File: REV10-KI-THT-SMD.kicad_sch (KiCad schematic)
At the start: 40 parts, among them J1 EJ508A (PWR), J2 54-00298, P1 SPADE, P2 SPADE, Q1 2N3904, U1 NJM78M05FA, U2 LMC555CN, U3 STQ1HNK60R-AP, U4 STQ1HNK60R-AP, U5 TL5001AIP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

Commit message: first dual
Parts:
- C8: footprint THT-SMD:C_THT_SMD -> THT-SMD:CHV
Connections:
- net FINAL_SIGNAL: now also U6.P$6; no longer U6.P$17
- net GND: now also U6.P$26; no longer U6.P$10, U6.P$16
- no-connect marks 26 -> 27
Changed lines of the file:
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@@
 	)
 	(no_connect
-		(at 229.87 78.74)
+		(at 229.87 88.9)
 	)
 	(no_connect
-		(at 257.81 91.44)
+		(at 257.81 66.04)
 	)
 	(no_connect
@@
 		(at 229.87 91.44)
 	)
+	(no_connect
+		(at 257.81 68.58)
+	)
 	(wire
 		(pts
@@
 	(wire
 		(pts
-			(xy 257.81 66.04) (xy 260.35 66.04)
-		)
-		(stroke
-			(width 0)
-			(type default)
-		)
-	)
-	(wire
-		(pts
 			(xy 87.63 88.9) (xy 87.63 97.79)
 		)
@@
 	(wire
 		(pts
-			(xy 257.81 68.58) (xy 261.62 68.58)
-		)
-		(stroke
-			(width 0)
-			(type default)
-		)
-	)
-	(wire
-		(pts
 			(xy 247.65 129.54) (xy 247.65 127)
 		)
@@
 	(wire
 		(pts
+			(xy 226.06 78.74) (xy 229.87 78.74)
+		)
+		(stroke
+			(width 0)
+			(type default)
+		)
+	)
+	(wire
+		(pts
 			(xy 88.9 121.92) (xy 93.98 121.92)
 		)
@@
 	(wire
 		(pts
-			(xy 143.51 78.74) (xy 143.51 87.63)
+			(xy 257.81 91.44) (xy 260.35 91.44)
 		)
 		(stroke
@@
 	(wire
 		(pts
-			(xy 227.33 88.9) (xy 229.87 88.9)
+			(xy 143.51 78.74) (xy 143.51 87.63)
 		)
 		(stroke
@@
 	(global_label "FINAL_SIGNAL"
 		(shape input)
-		(at 261.62 68.58 270)
+		(at 226.06 78.74 90)
 		(fields_autoplaced yes)
 		(effects
@@
 				(size 1.27 1.27)
 			)
-			(justify right)
+			(justify left)
 		)
 		(property "Intersheetrefs" "${INTERSHEET_REFS}"
-			(at 261.62 84.2049 90)
+			(at 226.06 63.1151 90)
 			(effects
 				(font
 					(size 1.27 1.27)
 				)
-				(justify right)
+				(justify left)
 				(hide yes)
 			)
@@
 			)
 		)
-		(property "Footprint" "THT-SMD:C_THT_SMD"
+		(property "Footprint" "THT-SMD:CHV"
 			(at 187.6552 115.57 0)
 			(effects
@@
 	(symbol
 		(lib_id "power:GND")
-		(at 260.35 66.04 90)
+		(at 260.35 91.44 90)
 		(unit 1)
 		(exclude_from_sim no)
@@
 		(on_board yes)
 		(dnp no)
-		(property "Reference" "#PWR031"
-			(at 266.7 66.04 0)
+		(property "Reference" "#PWR030"
+			(at 266.7 91.44 0)
 			(effects
 				(font
@@
 		)
 		(property "Value" "GND"
-			(at 259.588 62.992 90)
+			(at 259.588 88.392 90)
 			(effects
 				(font
@@
 		)
 		(property "Footprint" ""
-			(at 260.35 66.04 0)
+			(at 260.35 91.44 0)
 			(effects
 				(font
@@
 		)
 		(property "Datasheet" ""
-			(at 260.35 66.04 0)
+			(at 260.35 91.44 0)
 			(effects
 				(font
@@
 		)
 		(property "Description" "Power symbol creates a global label with name \"GND\" , ground"
-			(at 260.35 66.04 0)
+			(at 260.35 91.44 0)
 			(effects
 				(font
@@
 			(project ""
 				(path "/1dd91c79-34a0-4360-87fe-a0c6a402bed6"
-					(reference "#PWR031")
+					(reference "#PWR030")
 					(unit 1)
 				)
@@
 		(on_board yes)
 		(dnp no)
-		(property "Reference" "#PWR030"
+		(property "Reference" "#PWR029"
 			(at 260.35 137.16 0)
 			(effects
@@
 			(project ""
 				(path "/1dd91c79-34a0-4360-87fe-a0c6a402bed6"
-					(reference "#PWR030")
+					(reference "#PWR029")
 					(unit 1)
 				)
@@
 	)
 	(symbol
-		(lib_id "power:GND")
-		(at 227.33 88.9 270)
-		(unit 1)
-		(exclude_from_sim no)
-		(in_bom yes)
-		(on_board yes)
-		(dnp no)
-		(property "Reference" "#PWR028"
-			(at 220.98 88.9 0)
-			(effects
-				(font
-					(size 1.27 1.27)
-				)
-				(hide yes)
-			)
-		)
-		(property "Value" "GND"
-			(at 228.6 85.344 90)
-			(effects
-				(font
-					(size 1.27 1.27)
-				)
-				(justify right)
-			)
-		)
-		(property "Footprint" ""
-			(at 227.33 88.9 0)
-			(effects
-				(font
-					(size 1.27 1.27)
-				)
-				(hide yes)
-			)
-		)
-		(property "Datasheet" ""
-			(at 227.33 88.9 0)
-			(effects
-				(font
-					(size 1.27 1.27)
-				)
-				(hide yes)
-			)
-		)
-		(property "Description" "Power symbol creates a global label with name \"GND\" , ground"
-			(at 227.33 88.9 0)
-			(effects
-				(font
-					(size 1.27 1.27)
-				)
-				(hide yes)
-			)
-		)
-		(pin "1"
-		)
-		(instances
-			(project ""
-				(path "/1dd91c79-34a0-4360-87fe-a0c6a402bed6"
-					(reference "#PWR028")
-					(unit 1)
-				)
-			)
-		)
-	)
-	(symbol
 		(lib_id "REV9-KI:36-3530-ND")
 		(at 210.82 96.52 0)
@@
 		(on_board yes)
 		(dnp no)
-		(property "Reference" "#PWR029"
+		(property "Reference" "#PWR028"
 			(at 231.14 96.52 0)
 			(effects
@@
 			(project "REV9-KI"
 				(path "/1dd91c79-34a0-4360-87fe-a0c6a402bed6"
-					(reference "#PWR029")
+					(reference "#PWR028")
 					(unit 1)
 				)

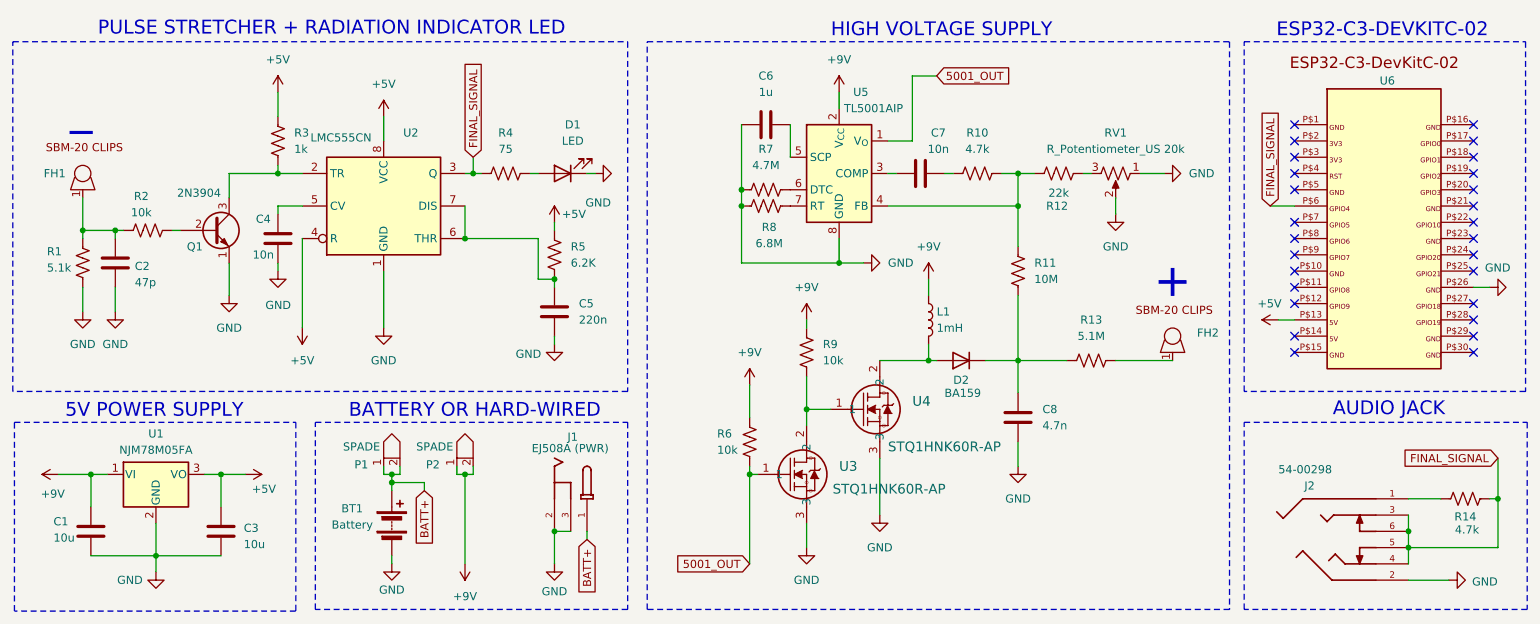
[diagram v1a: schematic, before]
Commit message: added holes for m4011, removed rev 9 backups
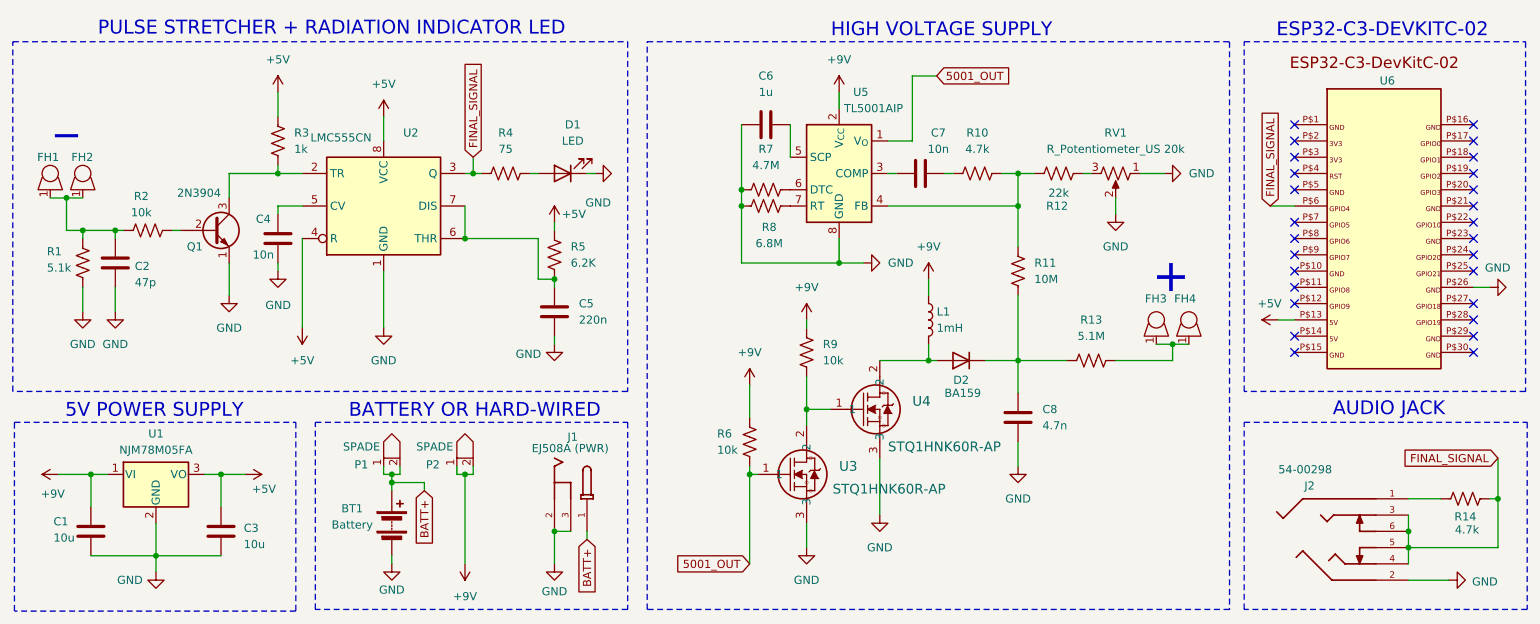
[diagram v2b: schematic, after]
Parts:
- added FH1, FH3: ~, 36-3530-ND:36-3530-ND, symbol REV9-KI:36-3530-ND
- renumbered FH1 to FH2, FH2 to FH4
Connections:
- net at C2.1, FH2.1, R1.1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: now also FH1.1
- net at FH4.1, R13.2: now also FH3.1
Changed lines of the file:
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@@
 	)
 	(junction
+		(at 38.1 77.47)
+		(diameter 0)
+		(color 0 0 0 0)
+	)
+	(junction
 		(at 247.65 129.54)
 		(diameter 0)
@@
 	)
 	(junction
+		(at 210.82 100.33)
+		(diameter 0)
+		(color 0 0 0 0)
+	)
+	(junction
 		(at 62.23 120.65)
 		(diameter 0)
@@
 	(wire
 		(pts
+			(xy 35.56 77.47) (xy 38.1 77.47)
+		)
+		(stroke
+			(width 0)
+			(type default)
+		)
+	)
+	(wire
+		(pts
 			(xy 100.33 73.66) (xy 101.6 73.66)
 		)
@@
 	(wire
 		(pts
+			(xy 38.1 77.47) (xy 40.64 77.47)
+		)
+		(stroke
+			(width 0)
+			(type default)
+		)
+	)
+	(wire
+		(pts
 			(xy 186.69 115.57) (xy 186.69 119.38)
 		)
@@
 	(wire
 		(pts
+			(xy 38.1 82.55) (xy 40.64 82.55)
+		)
+		(stroke
+			(width 0)
+			(type default)
+		)
+	)
+	(wire
+		(pts
 			(xy 196.85 73.66) (xy 198.12 73.66)
 		)
@@
 	(wire
 		(pts
+			(xy 208.28 100.33) (xy 210.82 100.33)
+		)
+		(stroke
+			(width 0)
+			(type default)
+		)
+	)
+	(wire
+		(pts
 			(xy 40.64 82.55) (xy 45.72 82.55)
 		)
@@
 	(wire
 		(pts
+			(xy 201.93 102.87) (xy 210.82 102.87)
+		)
+		(stroke
+			(width 0)
+			(type default)
+		)
+	)
+	(wire
+		(pts
+			(xy 210.82 100.33) (xy 210.82 102.87)
+		)
+		(stroke
+			(width 0)
+			(type default)
+		)
+	)
+	(wire
+		(pts
 			(xy 88.9 123.19) (xy 88.9 121.92)
 		)
@@
 	(wire
 		(pts
+			(xy 210.82 100.33) (xy 213.36 100.33)
+		)
+		(stroke
+			(width 0)
+			(type default)
+		)
+	)
+	(wire
+		(pts
 			(xy 101.6 120.65) (xy 101.6 119.38)
 		)
@@
 	(wire
 		(pts
-			(xy 40.64 77.47) (xy 40.64 82.55)
+			(xy 38.1 77.47) (xy 38.1 82.55)
 		)
 		(stroke
@@
 	(wire
 		(pts
-			(xy 201.93 102.87) (xy 210.82 102.87)
-		)
-		(stroke
-			(width 0)
-			(type default)
-		)
-	)
-	(wire
-		(pts
 			(xy 181.61 102.87) (xy 186.69 102.87)
 		)
@@
 	(text "_"
 		(exclude_from_sim no)
-		(at 40.386 63.754 0)
+		(at 38.1 64.262 0)
 		(effects
 			(font
@@
 	(text "+"
 		(exclude_from_sim no)
-		(at 210.82 90.678 0)
+		(at 210.566 89.916 0)
 		(effects
 			(font
@@
 	)
 	(symbol
+		(lib_id "REV9-KI:36-3530-ND")
+		(at 208.28 93.98 0)
+		(unit 1)
+		(exclude_from_sim no)
+		(in_bom yes)
+		(on_board yes)
+		(dnp no)
+		(property "Reference" "FH3"
+			(at 206.502 93.218 0)
+			(effects
+				(font
+					(size 1.27 1.27)
+				)
+				(justify left)
+			)
+		)
+		(property "Value" "~"
+			(at 217.17 96.5172 0)
+			(effects
+				(font
+					(size 1.27 1.27)
+				)
+				(justify left)
+			)
+		)
+		(property "Footprint" "36-3530-ND:36-3530-ND"
+			(at 208.28 93.98 0)
+			(effects
+				(font
+					(size 1.27 1.27)
+				)
+				(hide yes)
+			)
+		)
+		(property "Datasheet" ""
+			(at 208.28 93.98 0)
+			(effects
+				(font
+					(size 1.27 1.27)
+				)
+				(hide yes)
+			)
+		)
+		(property "Description" ""
+			(at 208.28 93.98 0)
+			(effects
+				(font
+					(size 1.27 1.27)
+				)
+				(hide yes)
+			)
+		)
+		(pin "1"
+		)
+		(instances
+			(project ""
+				(path "/1dd91c79-34a0-4360-87fe-a0c6a402bed6"
+					(reference "FH3")
+					(unit 1)
+				)
+			)
+		)
+	)
+	(symbol
 		(lib_id "0197084013:0197084013")
 		(at 88.9 116.84 0)
@@
 		(on_board yes)
 		(dnp no)
-		(property "Reference" "FH1"
-			(at 34.544 73.66 0)
+		(property "Reference" "FH2"
+			(at 38.862 71.12 0)
 			(effects
 				(font
@@
 			(project ""
 				(path "/1dd91c79-34a0-4360-87fe-a0c6a402bed6"
-					(reference "FH1")
+					(reference "FH2")
 					(unit 1)
 				)
@@
 	(symbol
 		(lib_id "REV9-KI:36-3530-ND")
-		(at 210.82 96.52 0)
+		(at 213.36 93.98 0)
 		(unit 1)
 		(exclude_from_sim no)
@@
 		(on_board yes)
 		(dnp no)
-		(property "Reference" "FH2"
-			(at 214.63 98.552 0)
+		(property "Reference" "FH4"
+			(at 211.074 93.218 0)
 			(effects
 				(font
@@
 		)
 		(property "Value" "~"
-			(at 219.71 99.0572 0)
+			(at 222.25 96.5172 0)
 			(effects
 				(font
@@
 		)
 		(property "Footprint" "36-3530-ND:36-3530-ND"
-			(at 210.82 96.52 0)
+			(at 213.36 93.98 0)
 			(effects
 				(font
@@
 		)
 		(property "Datasheet" ""
-			(at 210.82 96.52 0)
+			(at 213.36 93.98 0)
 			(effects
 				(font
@@
 		)
 		(property "Description" ""
-			(at 210.82 96.52 0)
+			(at 213.36 93.98 0)
 			(effects
 				(font
@@
 			(project ""
 				(path "/1dd91c79-34a0-4360-87fe-a0c6a402bed6"
-					(reference "FH2")
+					(reference "FH4")
 					(unit 1)
 				)
@@
 					(unit 1)
 				)
+			)
+		)
+	)
+	(symbol
+		(lib_id "REV9-KI:36-3530-ND")
+		(at 35.56 71.12 0)
+		(unit 1)
+		(exclude_from_sim no)
+		(in_bom yes)
+		(on_board yes)
+		(dnp no)
+		(property "Reference" "FH1"
+			(at 33.528 71.12 0)
+			(effects
+				(font
+					(size 1.27 1.27)
+				)
+				(justify left)
+			)
+		)
+		(property "Value" "~"
+			(at 44.45 73.6572 0)
+			(effects
+				(font
+					(size 1.27 1.27)
+				)
+				(justify left)
+			)
+		)
+		(property "Footprint" "36-3530-ND:36-3530-ND"
+			(at 35.56 71.12 0)
+			(effects
+				(font
+					(size 1.27 1.27)
+				)
+				(hide yes)
+			)
+		)
+		(property "Datasheet" ""
+			(at 35.56 71.12 0)
+			(effects
+				(font
+					(size 1.27 1.27)
+				)
+				(hide yes)
+			)
+		)
+		(property "Description" ""
+			(at 35.56 71.12 0)
+			(effects
+				(font
+					(size 1.27 1.27)
+				)
+				(hide yes)
+			)
+		)
+		(pin "1"
+		)
+		(instances
+			(project ""
+				(path "/1dd91c79-34a0-4360-87fe-a0c6a402bed6"
+					(reference "FH1")
+					(unit 1)
+				)

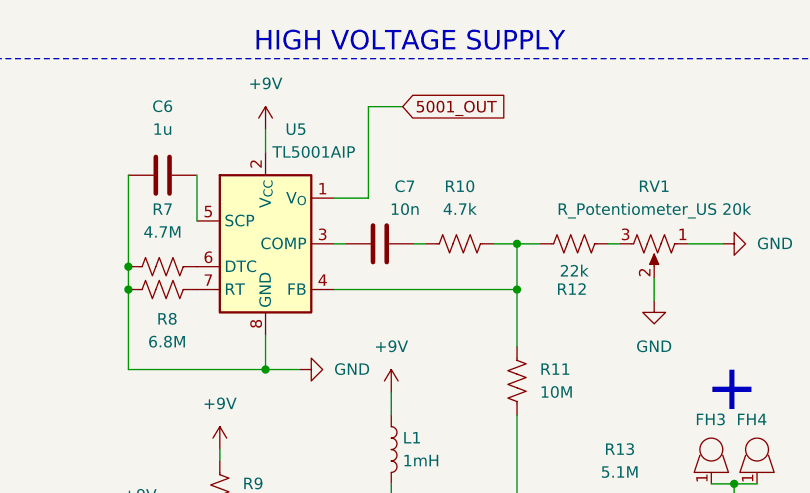
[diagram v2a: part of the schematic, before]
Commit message: changed 10nf to 15nf, realized the old design had that cap as 15, trying to stay true
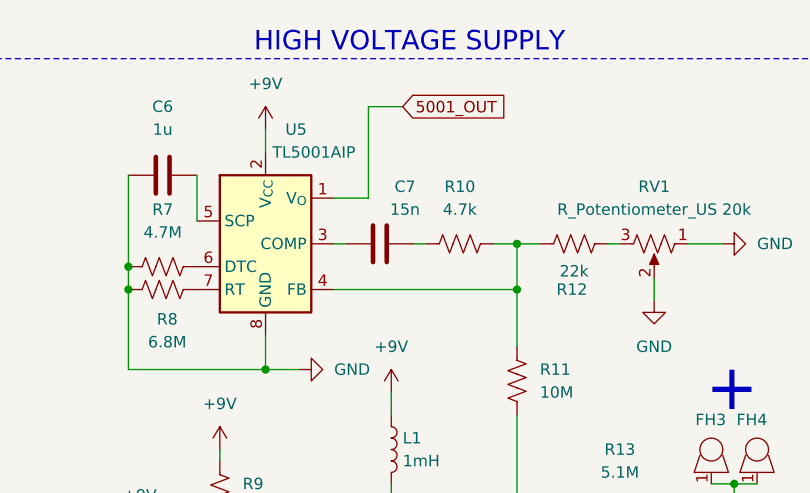
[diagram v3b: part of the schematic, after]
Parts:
- C7: value 10n -> 15n
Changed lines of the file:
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@@
 			)
 		)
-		(property "Value" "10n"
+		(property "Value" "15n"
 			(at 174.244 69.85 90)
 			(effects
